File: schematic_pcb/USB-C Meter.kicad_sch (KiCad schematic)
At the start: 11 parts, among them J1 USB_C_Receptacle_PowerOnly_6P, J2 USB_C_Receptacle_PowerOnly_6P, U1 WEMOS_D1_mini, U2 INA226, U3 Display I2C

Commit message: feat: pcb/schematic v2.1.0
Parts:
- removed C2: 20µ, Capacitor_Tantalum_SMD:CP_EIA-6032-20_AVX-F, symbol PCM_Capacitor_AKL:CP_SMD_Tantalum_AVX-F_6032
- removed U1: WEMOS_D1_mini, RF_Module:WEMOS_D1_mini_light, symbol RF_Module:WEMOS_D1_mini
- added C1: 33µF/35V, Capacitor_SMD:CP_Elec_5x5.8, symbol Device:C_Polarized
- added C10, C12, C13, C16, C8: 0.1µ, Capacitor_SMD:C_0603_1608Metric, symbol Device:C
- added C11, C14: 1µ, Capacitor_SMD:C_0603_1608Metric, symbol Device:C
- added C15: 10n, Capacitor_SMD:C_0603_1608Metric, symbol Device:C
- added C17, C18: 1pF, Capacitor_SMD:C_0402_1005Metric, symbol Device:C
- added C2, C3: 10µF/10V, Capacitor_SMD:C_0603_1608Metric, symbol Device:C
- added C21: 0.1µF/6.3V, Capacitor_SMD:C_0603_1608Metric, symbol Device:C
- added C5: 10pF, Capacitor_SMD:C_0402_1005Metric, symbol Device:C
- added C6, C7: 220µF, Capacitor_SMD:CP_Elec_6.3x5.9, symbol Device:C_Polarized
- added C9: 10µF, Capacitor_SMD:C_0603_1608Metric, symbol Device:C
- added D1, D3, D4: 1N5819WS, Diode_SMD:D_SOD-323, symbol Diode:1N5819WS
- added D2: PMEG2005EH, Diode_SMD:D_SOD-123F, symbol Diode:PMEG2005EH
- added J1: USB_B_Micro, Connector_USB:USB_Micro-B_Wuerth_629105150521, symbol Connector:USB_B_Micro
- added J3: Generic IN, Connector_PinHeader_2.54mm:PinHeader_2x05_P2.54mm_Horizontal, symbol Connector_Generic:Conn_02x05_Odd_Even
- added J4: Generic OUT, Connector_PinSocket_2.54mm:PinSocket_2x05_P2.54mm_Horizontal, symbol Connector_Generic:Conn_02x05_Odd_Even
- added J6: Conn_Coaxial, Connector_Coaxial:U.FL_Hirose_U.FL-R-SMT-1_Vertical, symbol Connector:Conn_Coaxial
- added L1: 47µH, Inductor_SMD:L_Changjiang_FXL0630, symbol Device:L
- added L2: 2.7nH, Inductor_SMD:L_0603_1608Metric_Pad1.05x0.95mm_HandSolder, symbol Device:L
- added R11, R9: 10R, Resistor_SMD:R_0402_1005Metric, symbol Device:R
- added R12, R4: 12k, Resistor_SMD:R_0603_1608Metric_Pad0.98x0.95mm_HandSolder, symbol Device:R
- added R3: 400R, Resistor_SMD:R_0402_1005Metric, symbol Device:R
- added U1: XL1509-3.3, Package_SO:SOIC-8_3.9x4.9mm_P1.27mm, symbol Regulator_Switching:XL1509-3.3
- added U2: ME6211C33, Package_TO_SOT_SMD:SOT-23-5, symbol Regulator_Linear:ME6211C33M5
- added U3: TPS2115, Package_SO:TSSOP-8_4.4x3mm_P0.65mm, symbol TPS2115:TPS2115
- added U4: ESP32-C3FH4, Package_DFN_QFN:QFN-32-1EP_5x5mm_P0.5mm_EP3.7x3.7mm, symbol MCU_Espressif:ESP32-C3
- added Y1: 40MHz, Crystal:Crystal_SMD_3225-4Pin_3.2x2.5mm, symbol Device:Crystal_GND24
- C4: value 0.1µ -> 10pF; footprint Capacitor_SMD:C_0603_1608Metric -> Capacitor_SMD:C_0402_1005Metric
- J2: renamed from J1; value USB_C_Receptacle_PowerOnly_6P -> USB-C Receptacle 6P; footprint Connector_USB:USB_C_Receptacle_HRO_TYPE-C-31-M-17 -> Connector_USB:USB_C_Receptacle_GCT_USB4125-xx-x_6P_TopMnt_Horizontal
- J5: renamed from J2; value USB_C_Receptacle_PowerOnly_6P -> USB-C Receptacle 6P
- R10: renamed from R1; footprint Resistor_SMD:R_1206_3216Metric -> Resistor_SMD:R_2512_6332Metric
- U6: renamed from U2; value INA226 -> INA228
- U7: renamed from U3; footprint Connector_PinHeader_2.54mm:PinHeader_1x04_P2.54mm_Vertical -> Connector_PinSocket_2.54mm:PinSocket_1x04_P2.54mm_Vertical; symbol Display_Character:NHD-C0220BIZ -> Connector:Conn_01x04_Socket
- renumbered C3 to C20, R5 to R1, R4 to R2
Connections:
- net GND: now also C4.2, C1.2, C10.1, C11.2, C12.1, C13.1, C14.1, C15.1, C16.1, C2.2, C3.2, C5.1, C6.2, C7.2, C8.2, C9.2, D2.2 (A), J1.5 (GND), J1.6 (Shield), J3.2 (Pin_2), J3.4 (Pin_4), J3.7 (Pin_7), J3.9 (Pin_9), J4.2 (Pin_2), J4.4 (Pin_4), J4.7 (Pin_7), J4.9 (Pin_9), J6.2 (Ext), L2.1, R3.2, U1.4 (~{EN}), U1.5 (GND), U1.6 (GND), U1.7 (GND), U1.8 (GND), U2.2 (V_{SS}), U3.3 (D1), U3.5 (GND), U4.33 (GND), Y1.2, Y1.4; no longer C4.1
- net VBUS_PD_1_IN: now reaches J2.A9 (VBUS), J2.B9 (VBUS), R10.1
- net VBUS_PD_1_IN: now also D3.2 (A), J3.1 (Pin_1), J3.10 (Pin_10), J3.3 (Pin_3), J3.8 (Pin_8), R9.2; no longer U6.10 (Vin+)
- net 3V3: now reaches C20.1, R1.2, R2.2, U6.2 (A0), U6.6 (VS), U7.1 (Pin_1)
- net 3V3: now also C10.2, C11.1, C12.2, C14.2, C15.2, C7.1, C8.1, C9.1, R12.2, R4.2, U3.7 (OUT), U4.11 (VDD3P3_RTC), U4.17 (VDD3P3_CPU), U4.2 (VDD3P3), U4.3 (VDD3P3), U4.31 (VDDA), U4.32 (VDDA); no longer C4.2
- net SDA: now reaches R1.1, U6.4 (SDA)
- net SDA: now also U7.3 (Pin_3), U4.6 (GPIO2); no longer U7.4 (SDA)
- net SCL: now reaches R2.1, U6.5 (SCL)
- net SCL: now also U7.4 (Pin_4), U4.14 (GPIO8); no longer U7.3 (SCL)
- net SHNT-: now reaches U6.8 (Vbus), U6.9 (Vin-)
- net SHNT-: now also C21.2, R11.1
- net CC1: now reaches J2.A5 (CC1), J5.A5 (CC1)
- net VBUS_PD_2_IN: now reaches J5.A9 (VBUS), J5.B9 (VBUS), R10.2
- net VBUS_PD_2_IN: now also D4.2 (A), J4.1 (Pin_1), J4.10 (Pin_10), J4.3 (Pin_3), J4.8 (Pin_8), R11.2
- net CC2: now reaches J2.B5 (CC2), J5.B5 (CC2)
- new net: C16.2, R4.1, U4.7 (CHIP_EN)
- new net: J1.2 (D-), U4.25 (GPIO18)
- new net: J1.3 (D+), U4.26 (GPIO19)
- new net: C4.1, U4.29 (XTAL_N), Y1.1
- new net: C17.2, C18.2, L2.2
- new net: D2.1 (K), L1.1, U1.2 (OUT)
- new net: C13.2, U4.18 (VDD_SPI)
- new net: C5.2, U4.30 (XTAL_P), Y1.3
- new net: R12.1, U4.8 (GPIO3)
- new net: R3.1, U3.4 (ILIM)
- new net ANT: C18.1, J6.1 (In)
- new net CHGR_ID_GENERIC: J3.5 (Pin_5), J3.6 (Pin_6), J4.5 (Pin_5), J4.6 (Pin_6)
- new net RF: C17.1, U4.1 (LNA_IN)
- new net SHNT+: C21.1, R9.1, U6.10 (Vin+)
- new net VBUS_DATA_3V3: C3.1, U2.5 (V_{OUT}), U3.8 (IN1)
- new net VBUS_DATA_IN: D1.2 (A), J1.1 (VBUS)
- new net VBUS_DATA_R: C2.1, D1.1 (K), U2.1 (V_{IN}), U2.3 (CE)
- new net VBUS_PD_3V3: C6.1, L1.2, U1.3 (FB), U3.6 (IN2)
- new net VBUS_PD_R: C1.1, D3.1 (K), D4.1 (K), U1.1 (VIN)
- no-connect marks 0 -> 20
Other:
- company: Netwake -> Macwake.de
- moved on the sheet: C20, J2, J5, R1, R10, R2, U6

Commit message: feat: pcb/schematic v2.1.1
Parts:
- added J7: UART, Connector_PinHeader_1.00mm:PinHeader_1x04_P1.00mm_Vertical_SMD_Pin1Left, symbol Connector_Generic:Conn_01x04
- added R13, R14: 12k, Resistor_SMD:R_0603_1608Metric_Pad0.98x0.95mm_HandSolder, symbol Device:R
- added TP1: Boot, TestPoint:TestPoint_Pad_D1.5mm, symbol Connector:TestPoint
- added TP2: Expansion, TestPoint:TestPoint_Pad_D1.5mm, symbol Connector:TestPoint
- added TP3: Reset, TestPoint:TestPoint_Pad_D1.5mm, symbol Connector:TestPoint
- C4, C5: value 10pF -> 27pF
- D1, D3, D4: footprint Diode_SMD:D_SOD-323 -> Diode_SMD:D_SOD-123F
- R1, R2: footprint Resistor_SMD:R_0402_1005Metric -> Resistor_SMD:R_0603_1608Metric_Pad0.98x0.95mm_HandSolder
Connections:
- net 3V3: now also J7.4 (Pin_4), R13.2, R14.2
- net GND: now also J7.1 (Pin_1)
- net at C16.2, R4.1, U4.7 (CHIP_EN): now also TP3.1
- net at U4.15 (GPIO9): now also R13.1, TP1.1
- net at U4.16 (GPIO10): now also R14.1, TP2.1
- net at U4.27 (U0RXD): now also J7.2 (Pin_2)
- net at U4.28 (U0TXD): now also J7.3 (Pin_3)
- no-connect marks 20 -> 16
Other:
- moved on the sheet: C10, C11, C12, C13, C14, C15, C16, C17, C18, C4, C5, C8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

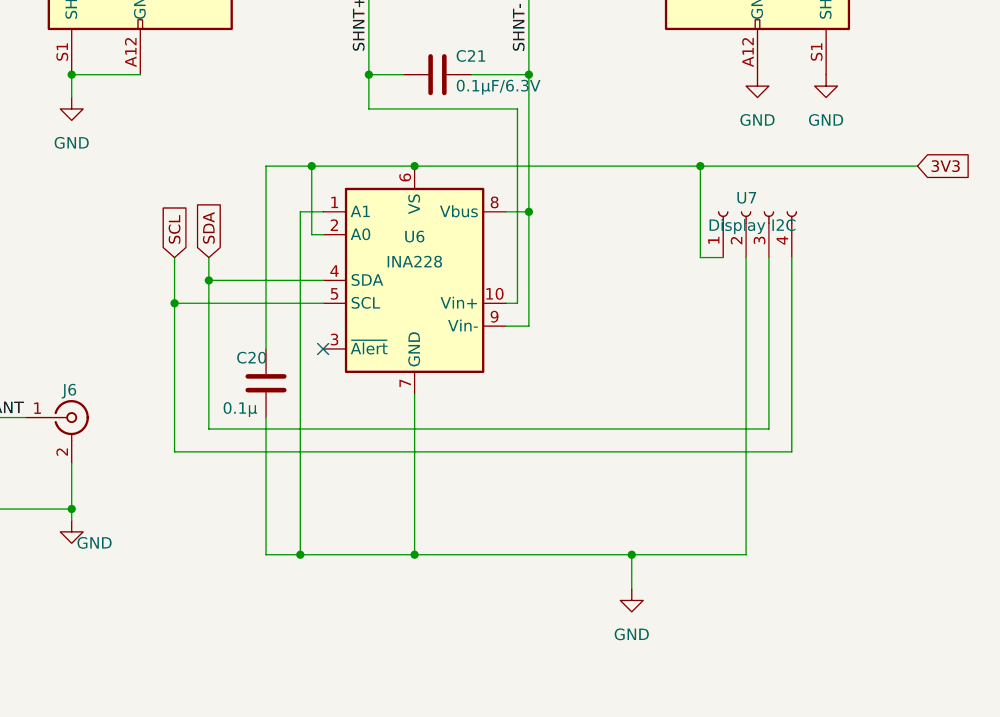
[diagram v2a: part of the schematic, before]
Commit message: fix(pcb): fixed sda/scl pin mismatch at display connector
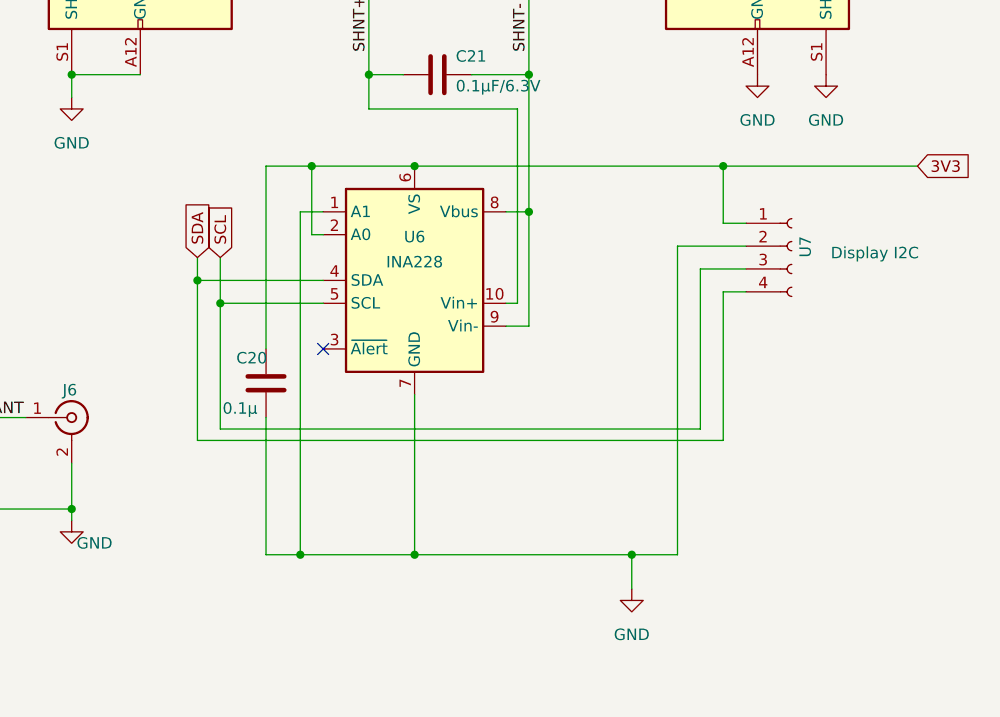
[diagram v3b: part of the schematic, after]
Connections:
- net SCL: now also U7.3 (Pin_3); no longer U7.4 (Pin_4)
- net SDA: now also U7.4 (Pin_4); no longer U7.3 (Pin_3)
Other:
- moved on the sheet: U7
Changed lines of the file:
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@@
 	(title_block
 		(title "USB-C Power Meter")
-		(date "2025-07-25")
-		(rev "2.1")
+		(date "2025-08-18")
+		(rev "2.2.2")
 		(company "Macwake.de")
 	)
@@
 	)
 	(junction
+		(at 222.25 106.68)
+		(diameter 0)
+		(color 0 0 0 0)
+	)
+	(junction
 		(at 63.5 105.41)
 		(diameter 0)
@@
 	)
 	(junction
+		(at 163.83 119.38)
+		(diameter 0)
+		(color 0 0 0 0)
+	)
+	(junction
 		(at 21.59 144.78)
 		(diameter 0)
@@
 	)
 	(junction
-		(at 165.1 119.38)
-		(diameter 0)
-		(color 0 0 0 0)
-	)
-	(junction
 		(at 132.08 134.62)
 		(diameter 0)
@@
 	)
 	(junction
-		(at 161.29 121.92)
-		(diameter 0)
-		(color 0 0 0 0)
-	)
-	(junction
 		(at 168.91 52.07)
 		(diameter 0)
@@
 	)
 	(junction
-		(at 219.71 106.68)
-		(diameter 0)
-		(color 0 0 0 0)
-	)
-	(junction
 		(at 140.97 26.67)
 		(diameter 0)
@@
 	)
 	(junction
+		(at 166.37 121.92)
+		(diameter 0)
+		(color 0 0 0 0)
+	)
+	(junction
 		(at 168.91 36.83)
 		(diameter 0)
@@
 	(wire
 		(pts
-			(xy 227.33 135.89) (xy 227.33 116.84)
-		)
-		(stroke
-			(width 0)
-			(type default)
-		)
-	)
-	(wire
-		(pts
 			(xy 88.9 105.41) (xy 81.28 105.41)
 		)
@@
 	(wire
 		(pts
-			(xy 212.09 149.86) (xy 224.79 149.86)
+			(xy 212.09 149.86) (xy 217.17 149.86)
 		)
 		(stroke
@@
 	(wire
 		(pts
+			(xy 222.25 120.65) (xy 222.25 137.16)
+		)
+		(stroke
+			(width 0)
+			(type default)
+		)
+	)
+	(wire
+		(pts
 			(xy 223.52 49.53) (xy 220.98 49.53)
 		)
@@
 	(wire
 		(pts
+			(xy 224.79 113.03) (xy 222.25 113.03)
+		)
+		(stroke
+			(width 0)
+			(type default)
+		)
+	)
+	(wire
+		(pts
 			(xy 204.47 71.12) (xy 210.82 71.12)
 		)
@@
 	(wire
 		(pts
+			(xy 222.25 106.68) (xy 243.84 106.68)
+		)
+		(stroke
+			(width 0)
+			(type default)
+		)
+	)
+	(wire
+		(pts
 			(xy 168.91 49.53) (xy 168.91 36.83)
 		)
@@
 	(wire
 		(pts
+			(xy 222.25 120.65) (xy 224.79 120.65)
+		)
+		(stroke
+			(width 0)
+			(type default)
+		)
+	)
+	(wire
+		(pts
 			(xy 116.84 139.7) (xy 113.03 139.7)
 		)
@@
 	(wire
 		(pts
-			(xy 219.71 106.68) (xy 243.84 106.68)
-		)
-		(stroke
-			(width 0)
-			(type default)
-		)
-	)
-	(wire
-		(pts
 			(xy 113.03 139.7) (xy 111.76 139.7)
 		)
@@
 	(wire
 		(pts
-			(xy 224.79 116.84) (xy 224.79 149.86)
-		)
-		(stroke
-			(width 0)
-			(type default)
-		)
-	)
-	(wire
-		(pts
 			(xy 152.4 52.07) (xy 152.4 54.61)
 		)
@@
 	(wire
 		(pts
-			(xy 229.87 138.43) (xy 229.87 116.84)
-		)
-		(stroke
-			(width 0)
-			(type default)
-		)
-	)
-	(wire
-		(pts
 			(xy 93.98 120.65) (xy 93.98 118.11)
 		)
@@
 	(wire
 		(pts
-			(xy 161.29 138.43) (xy 229.87 138.43)
+			(xy 166.37 135.89) (xy 219.71 135.89)
 		)
 		(stroke
@@
 	(wire
 		(pts
-			(xy 165.1 116.84) (xy 165.1 119.38)
+			(xy 163.83 116.84) (xy 163.83 119.38)
 		)
 		(stroke
@@
 	(wire
 		(pts
+			(xy 166.37 121.92) (xy 177.8 121.92)
+		)
+		(stroke
+			(width 0)
+			(type default)
+		)
+	)
+	(wire
+		(pts
 			(xy 195.58 26.67) (xy 140.97 26.67)
 		)
@@
 	(wire
 		(pts
-			(xy 161.29 138.43) (xy 161.29 121.92)
+			(xy 166.37 135.89) (xy 166.37 121.92)
 		)
 		(stroke
@@
 	(wire
 		(pts
-			(xy 161.29 116.84) (xy 161.29 121.92)
+			(xy 166.37 116.84) (xy 166.37 121.92)
 		)
 		(stroke
@@
 	(wire
 		(pts
+			(xy 217.17 115.57) (xy 217.17 149.86)
+		)
+		(stroke
+			(width 0)
+			(type default)
+		)
+	)
+	(wire
+		(pts
 			(xy 175.26 149.86) (xy 187.96 149.86)
 		)
@@
 	(wire
 		(pts
+			(xy 222.25 113.03) (xy 222.25 106.68)
+		)
+		(stroke
+			(width 0)
+			(type default)
+		)
+	)
+	(wire
+		(pts
+			(xy 217.17 115.57) (xy 224.79 115.57)
+		)
+		(stroke
+			(width 0)
+			(type default)
+		)
+	)
+	(wire
+		(pts
 			(xy 63.5 129.54) (xy 63.5 137.16)
 		)
@@
 	(wire
 		(pts
-			(xy 222.25 116.84) (xy 219.71 116.84)
+			(xy 219.71 118.11) (xy 219.71 135.89)
 		)
 		(stroke
@@
 	(wire
 		(pts
-			(xy 187.96 106.68) (xy 219.71 106.68)
+			(xy 187.96 106.68) (xy 222.25 106.68)
 		)
 		(stroke
@@
 	(wire
 		(pts
-			(xy 165.1 119.38) (xy 165.1 135.89)
+			(xy 163.83 119.38) (xy 163.83 137.16)
 		)
 		(stroke
@@
 	(wire
 		(pts
-			(xy 165.1 119.38) (xy 177.8 119.38)
+			(xy 173.99 52.07) (xy 168.91 52.07)
 		)
 		(stroke
@@
 	(wire
 		(pts
-			(xy 173.99 52.07) (xy 168.91 52.07)
+			(xy 182.88 96.52) (xy 182.88 100.33)
 		)
 		(stroke
@@
 	(wire
 		(pts
-			(xy 182.88 96.52) (xy 182.88 100.33)
+			(xy 93.98 129.54) (xy 93.98 128.27)
 		)
 		(stroke
@@
 	(wire
 		(pts
-			(xy 93.98 129.54) (xy 93.98 128.27)
+			(xy 153.67 52.07) (xy 152.4 52.07)
 		)
 		(stroke
@@
 	(wire
 		(pts
-			(xy 153.67 52.07) (xy 152.4 52.07)
+			(xy 171.45 149.86) (xy 175.26 149.86)
 		)
 		(stroke
@@
 	(wire
 		(pts
-			(xy 171.45 149.86) (xy 175.26 149.86)
+			(xy 21.59 143.51) (xy 21.59 144.78)
 		)
 		(stroke
@@
 	(wire
 		(pts
-			(xy 21.59 143.51) (xy 21.59 144.78)
+			(xy 199.39 121.92) (xy 198.12 121.92)
 		)
 		(stroke
@@
 	(wire
 		(pts
-			(xy 199.39 121.92) (xy 198.12 121.92)
+			(xy 163.83 137.16) (xy 222.25 137.16)
 		)
 		(stroke
@@
 	(wire
 		(pts
-			(xy 165.1 135.89) (xy 227.33 135.89)
+			(xy 163.83 119.38) (xy 177.8 119.38)
 		)
 		(stroke
@@
 	(wire
 		(pts
-			(xy 68.58 118.11) (xy 74.93 118.11)
+			(xy 219.71 118.11) (xy 224.79 118.11)
 		)
 		(stroke
@@
 	(wire
 		(pts
-			(xy 204.47 46.99) (xy 208.28 46.99)
+			(xy 68.58 118.11) (xy 74.93 118.11)
 		)
 		(stroke
@@
 	(wire
 		(pts
-			(xy 219.71 116.84) (xy 219.71 106.68)
+			(xy 204.47 46.99) (xy 208.28 46.99)
 		)
 		(stroke
@@
 	(wire
 		(pts
-			(xy 161.29 121.92) (xy 177.8 121.92)
-		)
-		(stroke
-			(width 0)
-			(type default)
-		)
-	)
-	(wire
-		(pts
 			(xy 88.9 107.95) (xy 88.9 128.27)
 		)
@@
 	(global_label "SCL"
 		(shape input)
-		(at 161.29 116.84 90)
+		(at 166.37 116.84 90)
 		(fields_autoplaced yes)
 		(effects
@@
 		)
 		(property "Intersheetrefs" "${INTERSHEET_REFS}"
-			(at 161.29 110.3472 90)
+			(at 166.37 110.3472 90)
 			(effects
 				(font
@@
 	(global_label "SDA"
 		(shape input)
-		(at 165.1 116.84 90)
+		(at 163.83 116.84 90)
 		(fields_autoplaced yes)
 		(effects
@@
 		)
 		(property "Intersheetrefs" "${INTERSHEET_REFS}"
-			(at 165.1 110.2867 90)
+			(at 163.83 110.2867 90)
 			(effects
 				(font
@@
 	(symbol
 		(lib_id "Connector:Conn_01x04_Socket")
-		(at 224.79 111.76 90)
+		(at 229.87 115.57 0)
 		(unit 1)
 		(exclude_from_sim no)
@@
 		(dnp no)
 		(property "Reference" "U7"
-			(at 226.06 110.236 90)
+			(at 231.394 116.84 90)
 			(effects
 				(font
@@
 		)
 		(property "Value" "Display I2C"
-			(at 230.378 113.284 90)
+			(at 234.188 116.332 0)
 			(effects
 				(font
@@
 		)
 		(property "Footprint" "Connector_PinSocket_2.54mm:PinSocket_1x04_P2.54mm_Vertical"
-			(at 224.79 111.76 0)
+			(at 229.87 115.57 0)
 			(effects
 				(font
@@
 		)
 		(property "Datasheet" "~"
-			(at 224.79 111.76 0)
+			(at 229.87 115.57 0)
 			(effects
 				(font
@@
 		)
 		(property "Description" "Generic connector, single row, 01x04, script generated"
-			(at 224.79 111.76 0)
+			(at 229.87 115.57 0)
 			(effects
 				(font
